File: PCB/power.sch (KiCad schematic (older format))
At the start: 15 parts

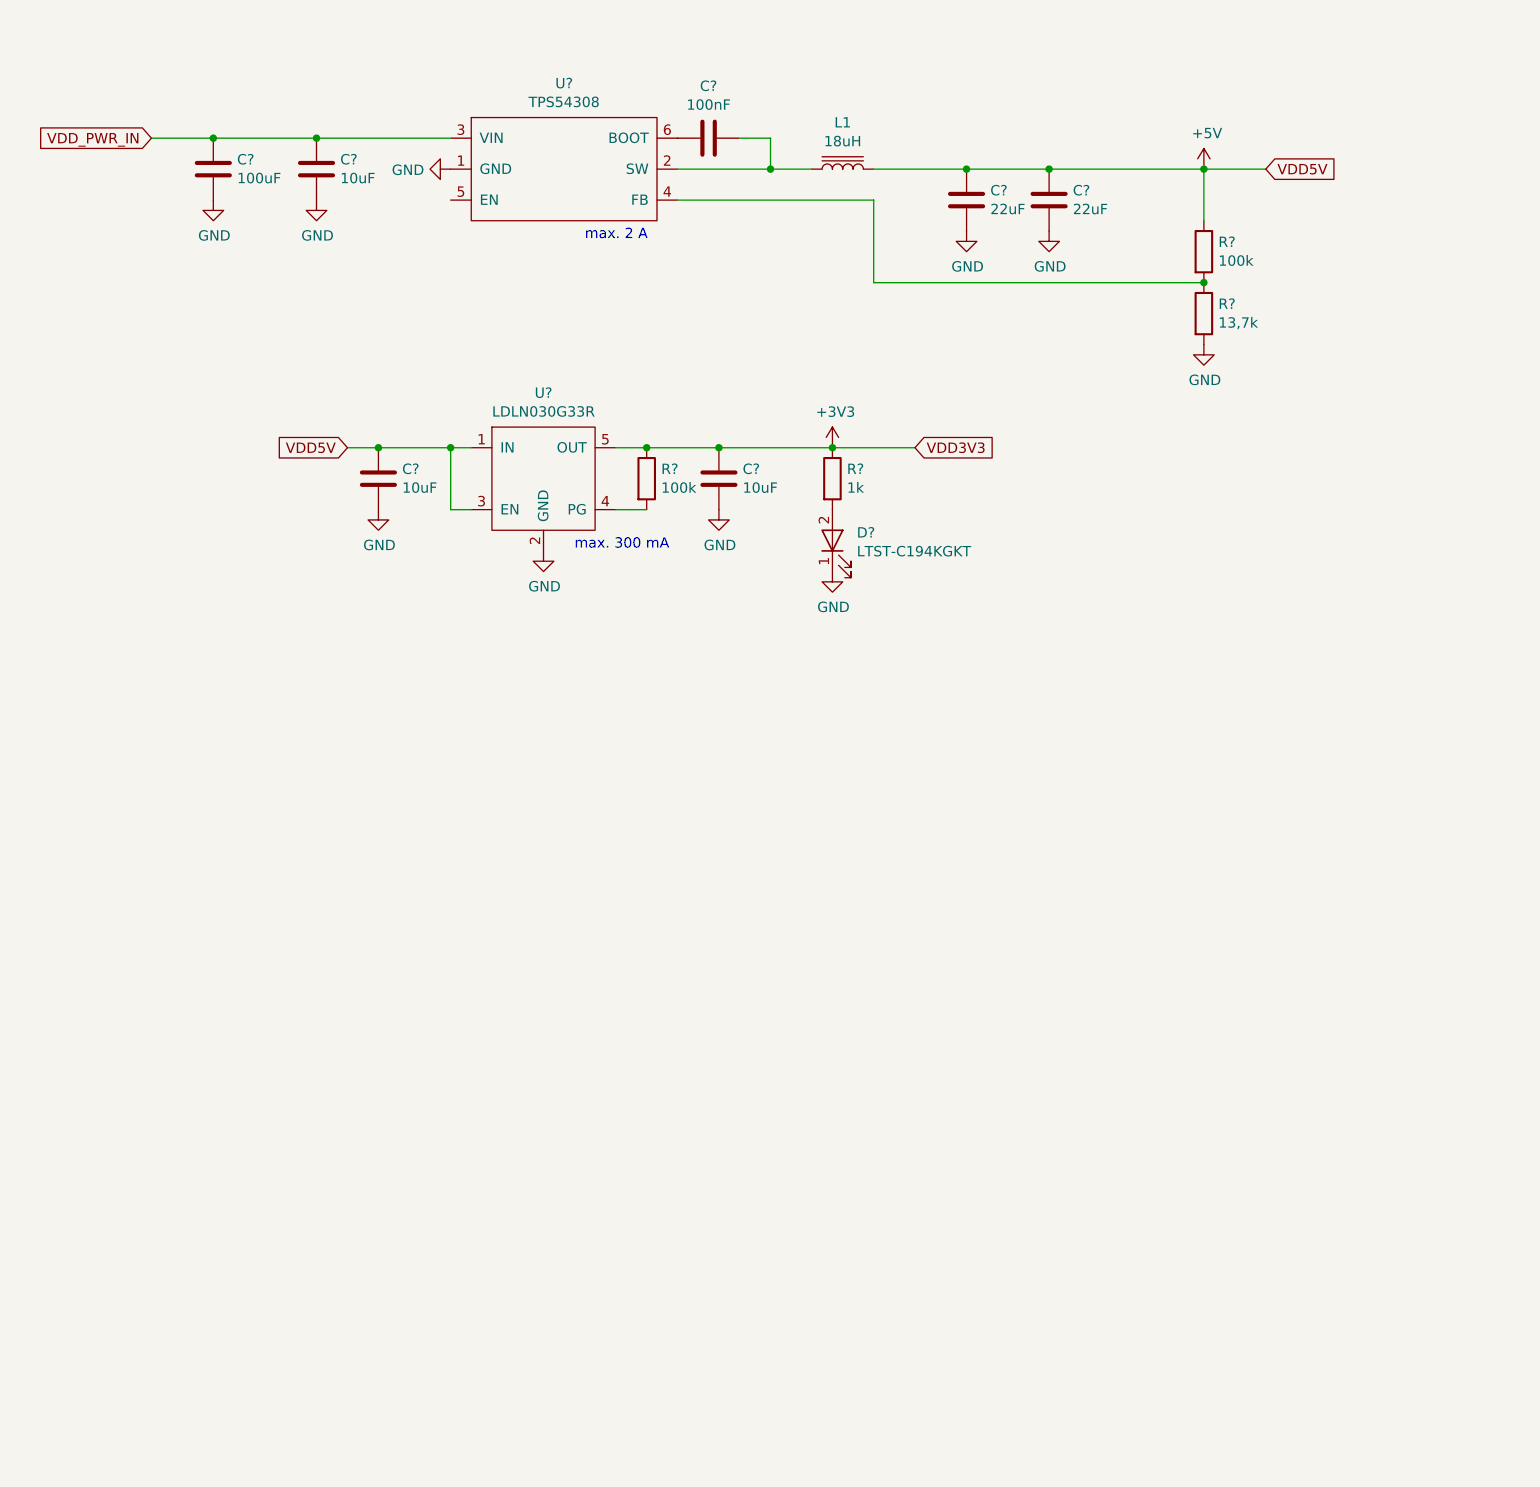
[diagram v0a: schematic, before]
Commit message: Changed PCB.
- Added MOSFET, connectors sheet
- Changed MCU and power sheet
- Reorganised sheets
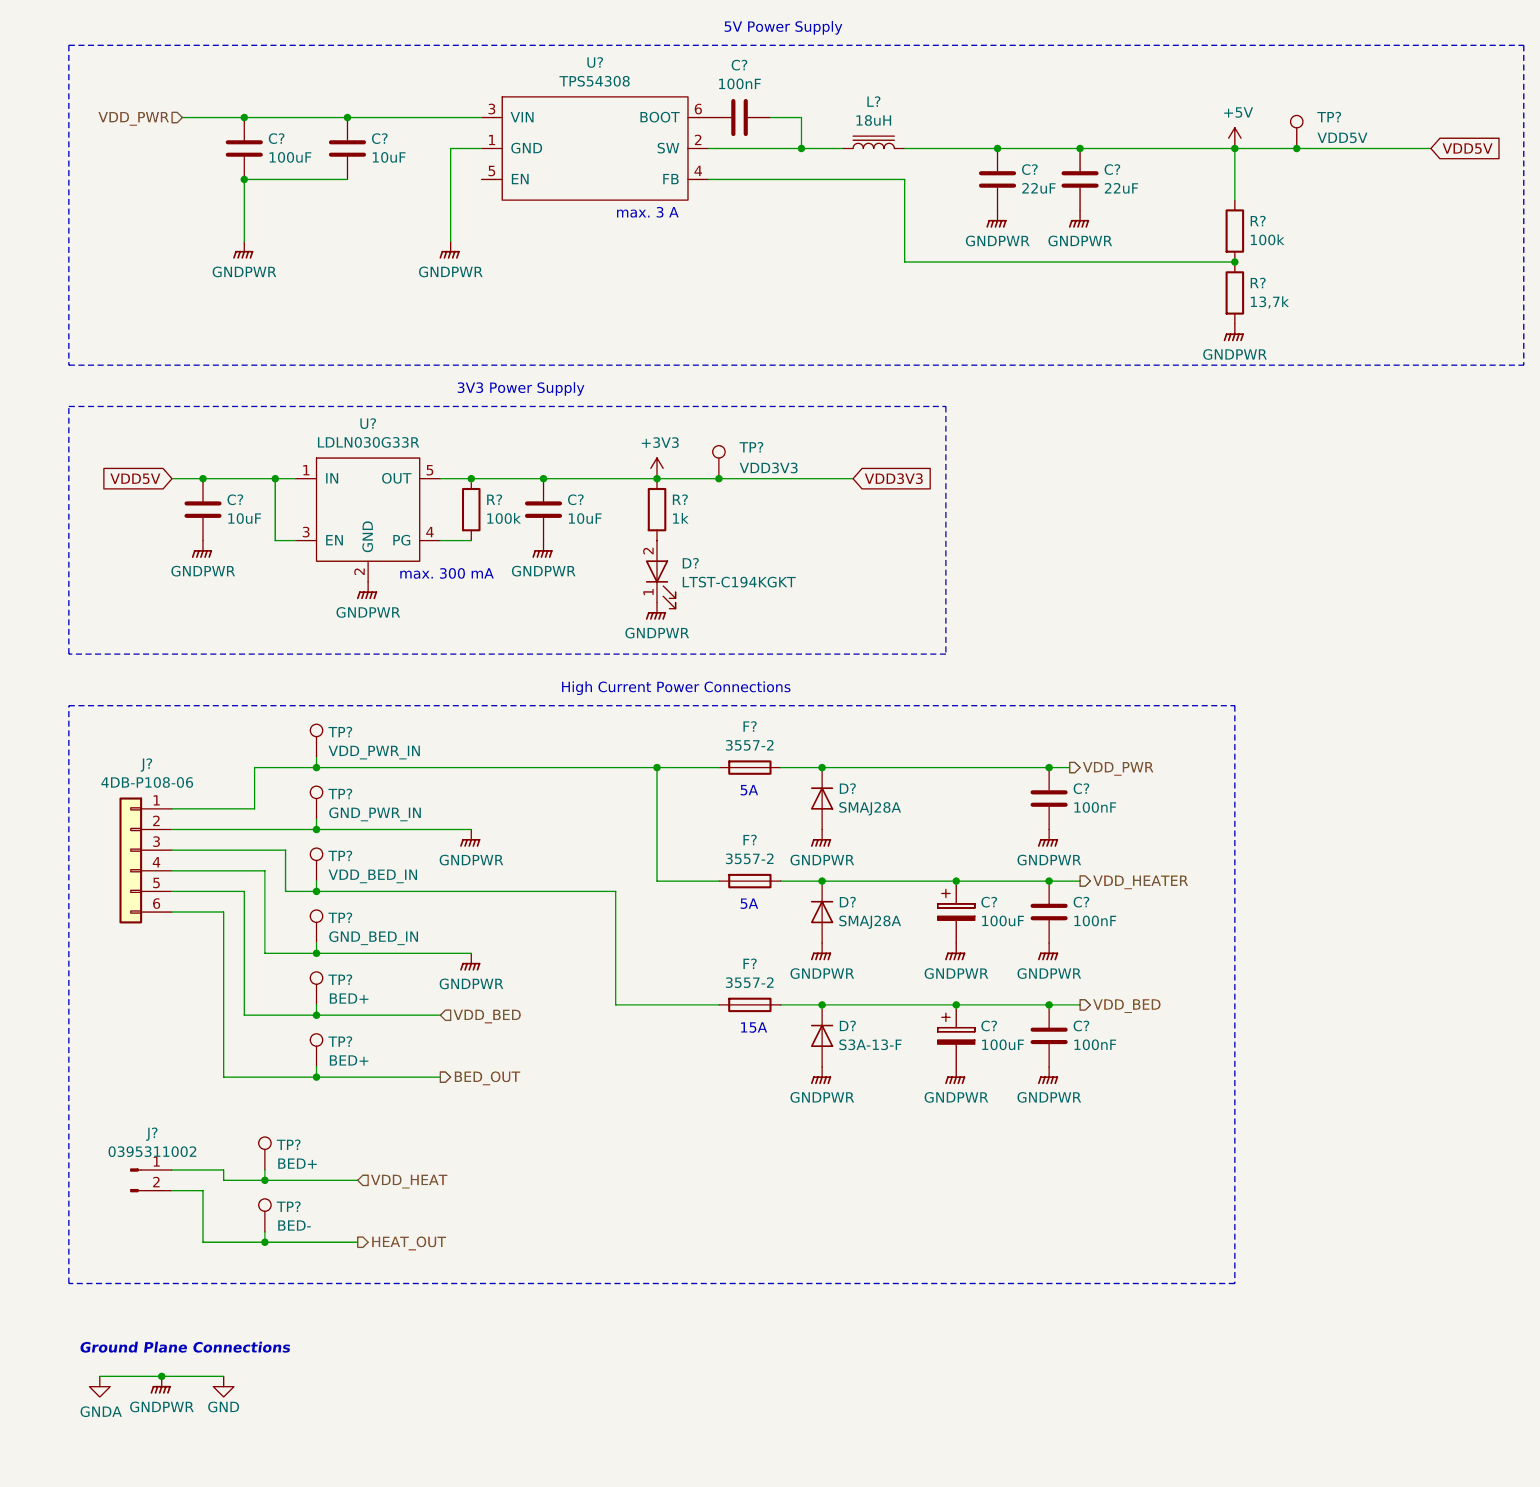
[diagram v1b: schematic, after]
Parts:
- added C? (x2): 100uF, Capacitor_THT:CP_Radial_D6.3mm_P2.50mm, symbol Device:CP
- added C? (x3): 100nF, Capacitor_SMD:C_1812_4532Metric, symbol Device:C
- added D? (x2): SMAJ28A, Diode_SMD:D_SMA, symbol Device:D
- added D?: S3A-13-F, Diode_SMD:D_SMC, symbol Device:D
- added F? (x3): 3557-2, custom-footprints:KEYSTONE-FUSE-3557-2, symbol Device:Fuse
- added J?: 4DB-P108-06, custom-footprints:4DB-P108-06, symbol Connector_Generic:Conn_01x06
- added J?: 0395311002, symbol Connector_Specialized:Conn_01x02_Male
- added TP?: GND_PWR_IN, symbol Connector_Specialized:Test_Point
- added TP?: VDD_PWR_IN, symbol Connector_Specialized:Test_Point
- added TP?: GND_BED_IN, symbol Connector_Specialized:Test_Point
- added TP?: VDD_BED_IN, symbol Connector_Specialized:Test_Point
- added TP?: BED-, symbol Connector_Specialized:Test_Point
- added TP? (x3): BED+, symbol Connector_Specialized:Test_Point
- added TP?: VDD5V, symbol Connector_Specialized:Test_Point
- added TP?: VDD3V3, symbol Connector_Specialized:Test_Point
- renumbered L1 to L?
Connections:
- net +3V3: now also TP?.1
- net +5V: now also TP?.1
- net GND: now also C?.2, C?.2, C?.2, C?.2, C?.2, D?.2 (A), D?.2 (A), D?.2 (A), J?.2 (Pin_2), J?.4 (Pin_4), TP?.1, TP?.1
- net VDD_PWR_IN renamed VDD_PWR
- net VDD_PWR: now also C?.1, D?.1 (K), F?.1
- new net: F?.2, F?.2, J?.1 (Pin_1), TP?.1
- new net: F?.2, J?.3 (Pin_3), TP?.1
- new net BED_OUT: J?.6 (Pin_6), TP?.1
- new net HEAT_OUT: J?.2 (Pin_2), TP?.1
- new net VDD_BED: C?.1, C?.1, D?.1 (K), F?.1, J?.5 (Pin_5), TP?.1
- new net VDD_HEAT: J?.1 (Pin_1), TP?.1
- new net VDD_HEATER: C?.1, C?.1, D?.1 (K), F?.1
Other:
- note added: "15A"
- note added: "3V3 Power Supply"
- note added: "5A"
- note added: "5V Power Supply"
- note added: "Ground Plane Connections"
- note added: "High Current Power Connections"
- note added: "max. 3 A"
- note removed: "max. 2 A"
- moved on the sheet: C?, D?, L?, R?, U?

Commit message: Changed some sheets and added LICENCE.
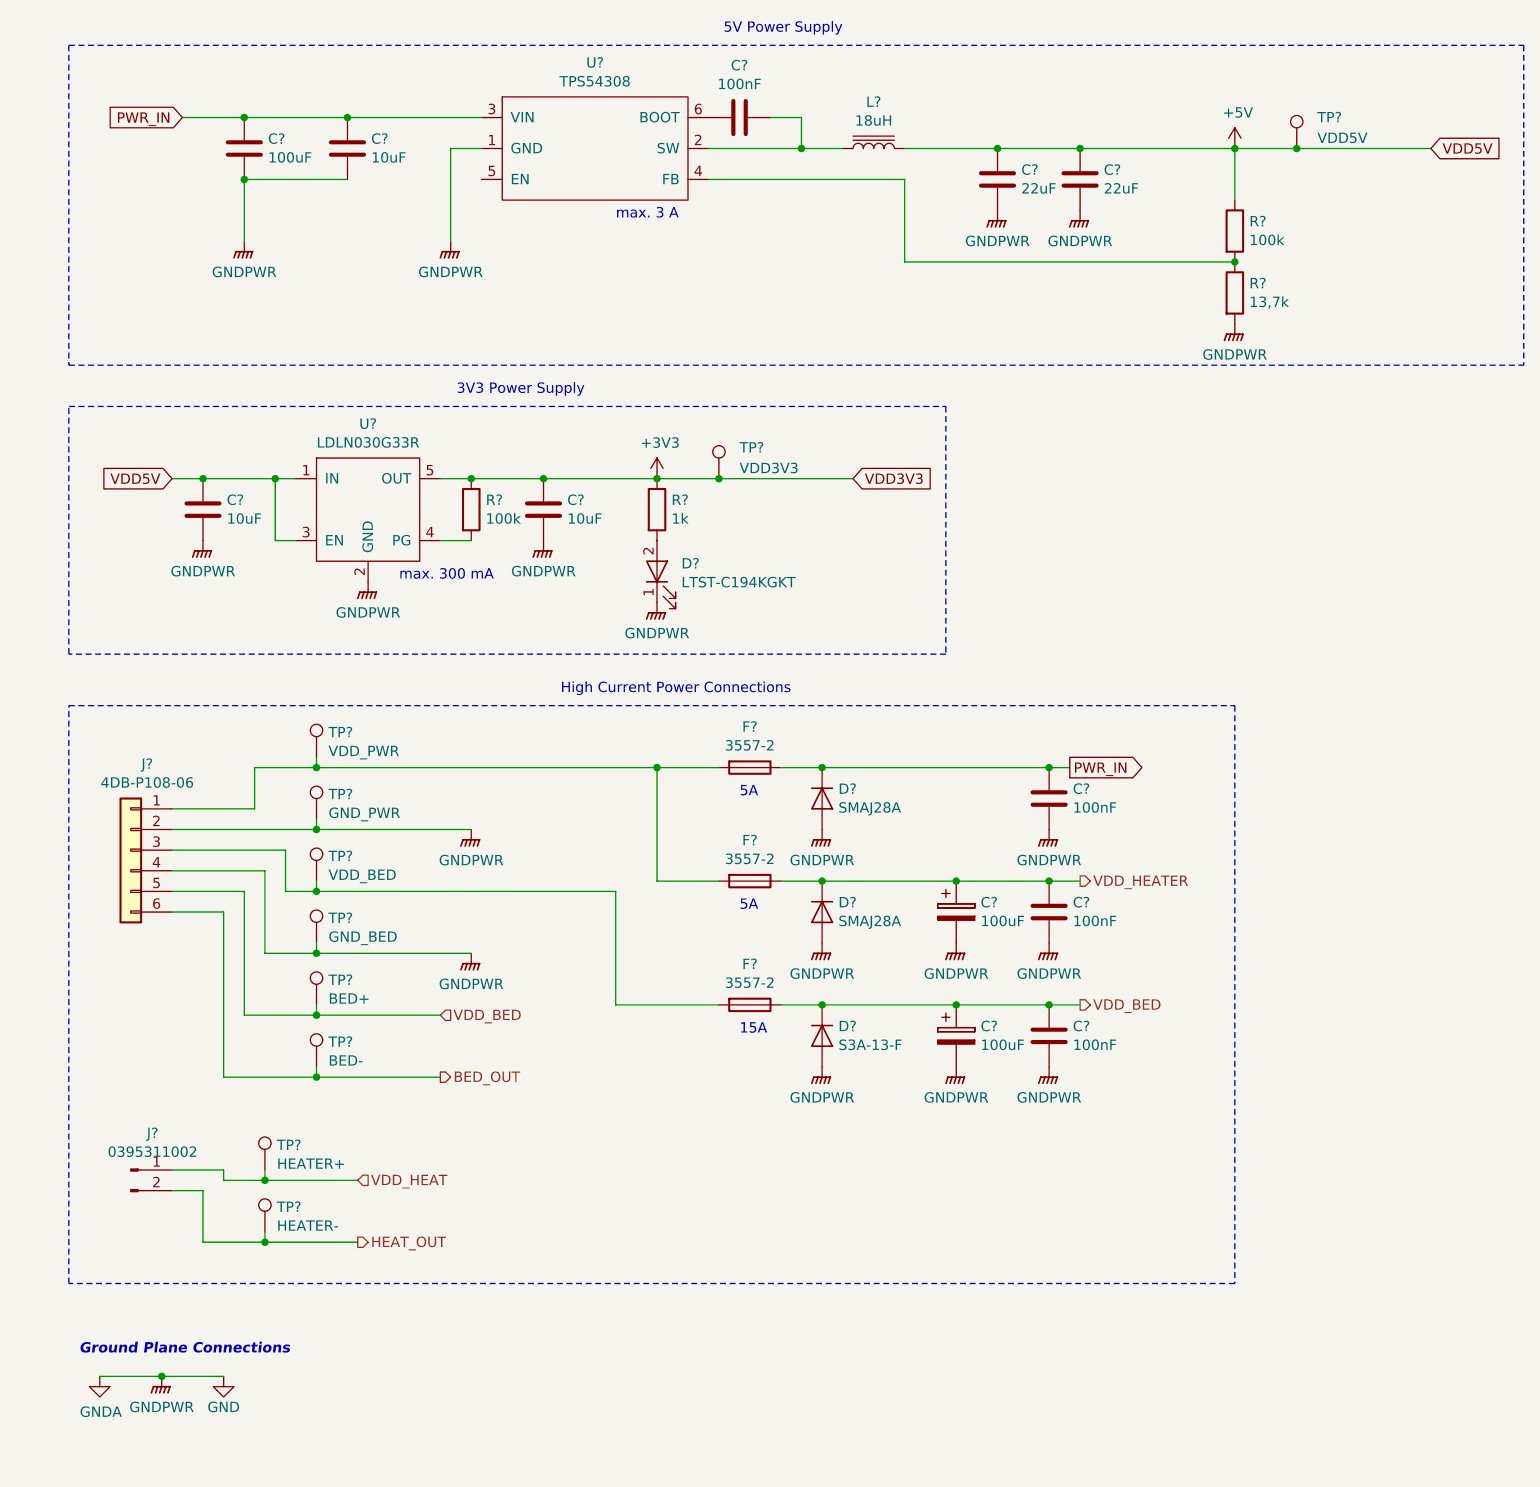
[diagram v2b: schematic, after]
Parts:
- TP?: value GND_PWR_IN -> GND_PWR; footprint (none) -> TestPoint:TestPoint_Pad_D1.0mm
- TP?: value VDD_PWR_IN -> VDD_PWR; footprint (none) -> TestPoint:TestPoint_Pad_D1.0mm
- TP?: value GND_BED_IN -> GND_BED; footprint (none) -> TestPoint:TestPoint_Pad_D1.0mm
- TP?: value VDD_BED_IN -> VDD_BED; footprint (none) -> TestPoint:TestPoint_Pad_D1.0mm
- TP?: value BED- -> HEATER-; footprint (none) -> TestPoint:TestPoint_Pad_D1.0mm
- TP? (x3): footprint (none) -> TestPoint:TestPoint_Pad_D1.0mm
- TP?: value BED+ -> HEATER+; footprint (none) -> TestPoint:TestPoint_Pad_D1.0mm
- TP?: value BED+ -> BED-; footprint (none) -> TestPoint:TestPoint_Pad_D1.0mm
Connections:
- net VDD_PWR renamed PWR_IN
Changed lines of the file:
@@
 $Descr A4 11693 8268
 encoding utf-8
-Sheet 7 5
+Sheet 3 5
 Title "Power"
 Date ""
@@
 P 1900 4400
 F 0 "TP?" H 1958 4520 50  0000 L CNN
-F 1 "GND_PWR_IN" H 1958 4429 50  0000 L CNN
-F 2 "" H 2100 4400 50  0001 C CNN
+F 1 "GND_PWR" H 1958 4429 50  0000 L CNN
+F 2 "TestPoint:TestPoint_Pad_D1.0mm" H 2100 4400 50  0001 C CNN
 F 3 "~" H 2100 4400 50  0001 C CNN
 	1    1900 4400
@@
 P 1900 4100
 F 0 "TP?" H 1958 4220 50  0000 L CNN
-F 1 "VDD_PWR_IN" H 1958 4129 50  0000 L CNN
-F 2 "" H 2100 4100 50  0001 C CNN
+F 1 "VDD_PWR" H 1958 4129 50  0000 L CNN
+F 2 "TestPoint:TestPoint_Pad_D1.0mm" H 2100 4100 50  0001 C CNN
 F 3 "~" H 2100 4100 50  0001 C CNN
 	1    1900 4100
@@
 P 1900 5000
 F 0 "TP?" H 1958 5120 50  0000 L CNN
-F 1 "GND_BED_IN" H 1958 5029 50  0000 L CNN
-F 2 "" H 2100 5000 50  0001 C CNN
+F 1 "GND_BED" H 1958 5029 50  0000 L CNN
+F 2 "TestPoint:TestPoint_Pad_D1.0mm" H 2100 5000 50  0001 C CNN
 F 3 "~" H 2100 5000 50  0001 C CNN
 	1    1900 5000
@@
 P 1900 4700
 F 0 "TP?" H 1958 4820 50  0000 L CNN
-F 1 "VDD_BED_IN" H 1958 4729 50  0000 L CNN
-F 2 "" H 2100 4700 50  0001 C CNN
+F 1 "VDD_BED" H 1958 4729 50  0000 L CNN
+F 2 "TestPoint:TestPoint_Pad_D1.0mm" H 2100 4700 50  0001 C CNN
 F 3 "~" H 2100 4700 50  0001 C CNN
 	1    1900 4700
@@
 P 1650 6400
 F 0 "TP?" H 1708 6520 50  0000 L CNN
-F 1 "BED-" H 1708 6429 50  0000 L CNN
-F 2 "" H 1850 6400 50  0001 C CNN
+F 1 "HEATER-" H 1708 6429 50  0000 L CNN
+F 2 "TestPoint:TestPoint_Pad_D1.0mm" H 1850 6400 50  0001 C CNN
 F 3 "~" H 1850 6400 50  0001 C CNN
 	1    1650 6400
@@
 F 0 "TP?" H 1958 5420 50  0000 L CNN
 F 1 "BED+" H 1958 5329 50  0000 L CNN
-F 2 "" H 2100 5300 50  0001 C CNN
+F 2 "TestPoint:TestPoint_Pad_D1.0mm" H 2100 5300 50  0001 C CNN
 F 3 "~" H 2100 5300 50  0001 C CNN
 	1    1900 5300
@@
 F 0 "TP?" H 6750 1300 50  0000 L CNN
 F 1 "VDD5V" H 6750 1200 50  0000 L CNN
-F 2 "" H 6850 1150 50  0001 C CNN
+F 2 "TestPoint:TestPoint_Pad_D1.0mm" H 6850 1150 50  0001 C CNN
 F 3 "~" H 6850 1150 50  0001 C CNN
 	1    6650 1150
@@
 F 0 "TP?" H 3950 2900 50  0000 L CNN
 F 1 "VDD3V3" H 3950 2800 50  0000 L CNN
-F 2 "" H 4050 2750 50  0001 C CNN
+F 2 "TestPoint:TestPoint_Pad_D1.0mm" H 4050 2750 50  0001 C CNN
 F 3 "~" H 4050 2750 50  0001 C CNN
 	1    3850 2750
@@
 Text HLabel 5600 4700 2    50   Output ~ 0
 VDD_HEATER
-Text HLabel 5550 4150 2    50   Output ~ 0
-VDD_PWR
-Text HLabel 1250 1000 0    50   Input ~ 0
-VDD_PWR
 Text HLabel 2500 5350 2    50   Input ~ 0
 VDD_BED
@@
 P 1650 6100
 F 0 "TP?" H 1708 6220 50  0000 L CNN
-F 1 "BED+" H 1708 6129 50  0000 L CNN
-F 2 "" H 1850 6100 50  0001 C CNN
+F 1 "HEATER+" H 1708 6129 50  0000 L CNN
+F 2 "TestPoint:TestPoint_Pad_D1.0mm" H 1850 6100 50  0001 C CNN
 F 3 "~" H 1850 6100 50  0001 C CNN
 	1    1650 6100
@@
 P 1900 5600
 F 0 "TP?" H 1958 5720 50  0000 L CNN
-F 1 "BED+" H 1958 5629 50  0000 L CNN
-F 2 "" H 2100 5600 50  0001 C CNN
+F 1 "BED-" H 1958 5629 50  0000 L CNN
+F 2 "TestPoint:TestPoint_Pad_D1.0mm" H 2100 5600 50  0001 C CNN
 F 3 "~" H 2100 5600 50  0001 C CNN
 	1    1900 5600
@@
 Text Notes 3200 2350 2    50   ~ 0
 3V3 Power Supply
+Text GLabel 1250 1000 0    50   Input ~ 0
+PWR_IN
+Text GLabel 5550 4150 2    50   Output ~ 0
+PWR_IN
 $EndSCHEMATC

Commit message: Finished first draft of the schematics.
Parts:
- added MK? (x4): Mounting_Hole_PAD, MountingHole:MountingHole_5.3mm_M5_ISO14580_Pad, symbol Mechanical:Mounting_Hole_PAD
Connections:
- net VDD_HEAT is gone; now on net VDD_HEATER: J?.1 (Pin_1), TP?.1
- net GND: now also MK?.1, MK?.1, MK?.1, MK?.1
- net PWR_IN renamed VDD_PWR
- no-connect marks 0 -> 1
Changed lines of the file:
@@
 $Descr A4 11693 8268
 encoding utf-8
-Sheet 3 5
+Sheet 3 9
 Title "Power"
 Date ""
@@
 $EndComp
 Text HLabel 2100 6150 2    50   Input ~ 0
-VDD_HEAT
+VDD_HEATER
 Text HLabel 2100 6450 2    50   Output ~ 0
 HEAT_OUT
@@
 Text Notes 3200 2350 2    50   ~ 0
 3V3 Power Supply
-Text GLabel 1250 1000 0    50   Input ~ 0
-PWR_IN
-Text GLabel 5550 4150 2    50   Output ~ 0
-PWR_IN
+$Comp
+L Mechanical:Mounting_Hole_PAD MK?
+U 1 1 5B0578B3
+P 2250 7250
+F 0 "MK?" H 2350 7301 50  0000 L CNN
+F 1 "Mounting_Hole_PAD" H 2350 7210 50  0000 L CNN
+F 2 "MountingHole:MountingHole_5.3mm_M5_ISO14580_Pad" H 2250 7250 50  0001 C CNN
+F 3 "" H 2250 7250 50  0001 C CNN
+	1    2250 7250
+	1    0    0    -1
+$EndComp
+$Comp
+L Mechanical:Mounting_Hole_PAD MK?
+U 1 1 5B0578BA
+P 3450 7250
+F 0 "MK?" H 3550 7301 50  0000 L CNN
+F 1 "Mounting_Hole_PAD" H 3550 7210 50  0000 L CNN
+F 2 "MountingHole:MountingHole_5.3mm_M5_ISO14580_Pad" H 3450 7250 50  0001 C CNN
+F 3 "" H 3450 7250 50  0001 C CNN
+	1    3450 7250
+	1    0    0    -1
+$EndComp
+$Comp
+L Mechanical:Mounting_Hole_PAD MK?
+U 1 1 5B0578C1
+P 4500 7250
+F 0 "MK?" H 4600 7301 50  0000 L CNN
+F 1 "Mounting_Hole_PAD" H 4600 7210 50  0000 L CNN
+F 2 "MountingHole:MountingHole_5.3mm_M5_ISO14580_Pad" H 4500 7250 50  0001 C CNN
+F 3 "" H 4500 7250 50  0001 C CNN
+	1    4500 7250
+	1    0    0    -1
+$EndComp
+$Comp
+L Mechanical:Mounting_Hole_PAD MK?
+U 1 1 5B0578C8
+P 5500 7250
+F 0 "MK?" H 5600 7301 50  0000 L CNN
+F 1 "Mounting_Hole_PAD" H 5600 7210 50  0000 L CNN
+F 2 "MountingHole:MountingHole_5.3mm_M5_ISO14580_Pad" H 5500 7250 50  0001 C CNN
+F 3 "" H 5500 7250 50  0001 C CNN
+	1    5500 7250
+	1    0    0    -1
+$EndComp
+$Comp
+L power:GNDPWR #PWR?
+U 1 1 5B0578CF
+P 4100 7350
+F 0 "#PWR?" H 4100 7150 50  0001 C CNN
+F 1 "GNDPWR" H 4100 7200 50  0000 C CNN
+F 2 "" H 4100 7300 50  0001 C CNN
+F 3 "" H 4100 7300 50  0001 C CNN
+	1    4100 7350
+	1    0    0    -1
+$EndComp
+Wire Wire Line
+	5500 7350 4500 7350
+Connection ~ 3450 7350
+Wire Wire Line
+	3450 7350 2250 7350
+Connection ~ 4100 7350
+Wire Wire Line
+	4100 7350 3450 7350
+Connection ~ 4500 7350
+Wire Wire Line
+	4500 7350 4100 7350
+NoConn ~ 2700 1300
+Text HLabel 5550 4150 2    50   Input ~ 0
+VDD_PWR
+Text HLabel 1250 1000 0    50   Input ~ 0
+VDD_PWR
 $EndSCHEMATC
